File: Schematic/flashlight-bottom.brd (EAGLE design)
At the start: 33.1 x 17.8 mm, 0 parts

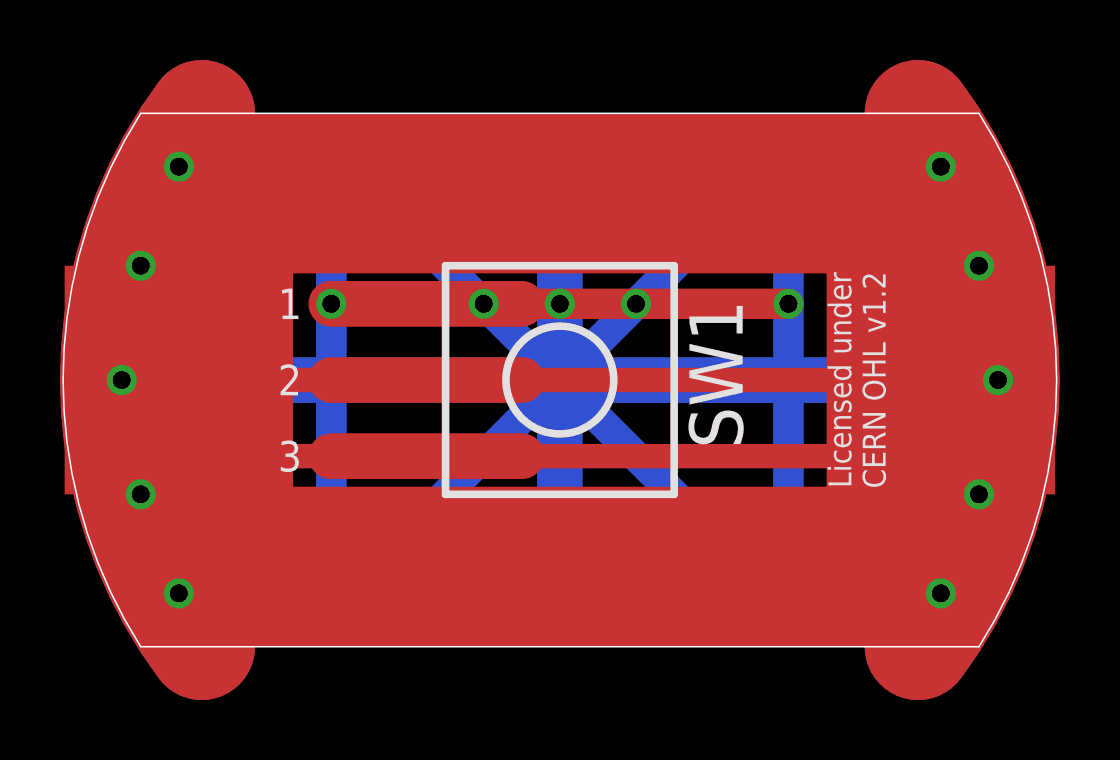
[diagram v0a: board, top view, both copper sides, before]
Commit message: Start revision 3.3 by adding a protection diode.
* Add a protection diode for the current regulator.
* Adjust the footprint of the switch to make it slightly easier
  to position and solder.
* Add text for the Diode to the documentation; however it should
  have updated pictures for the board throughout since this is
  more than a cosmetic change.
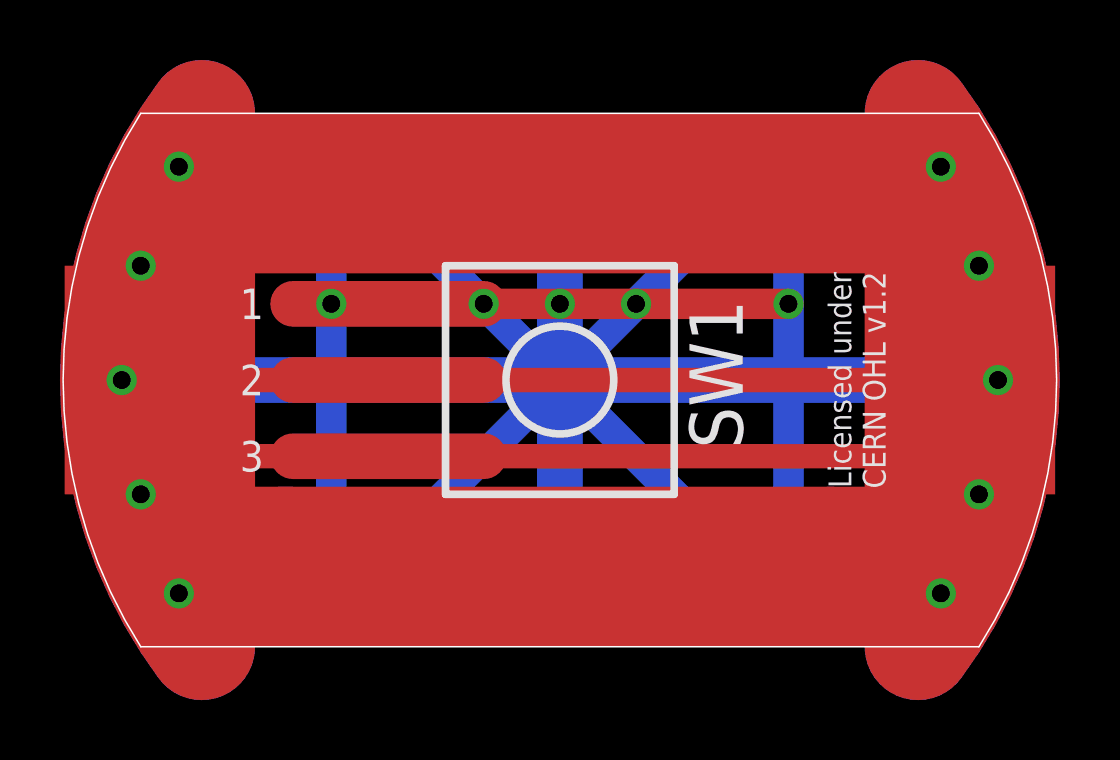
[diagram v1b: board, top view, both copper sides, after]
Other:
- board text added: "Bottom Board Rev. 3.3"
- board text removed: "Bottom Board Rev. 3.2"
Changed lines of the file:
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@@
 <?xml version="1.0" encoding="utf-8"?>
 <!DOCTYPE eagle SYSTEM "eagle.dtd">
-<eagle version="7.2.0">
+<eagle version="7.3.0">
 <drawing>
 <settings>
@@
 Flashlight</text>
 <text x="16.51" y="0.508" size="1.778" layer="29" ratio="15" align="bottom-center">Bottom Board
-Rev. 3.2</text>
+Rev. 3.3</text>
 <wire x1="16.51" y1="8.89" x2="8.89" y2="16.51" width="1.016" layer="30"/>
 <wire x1="16.51" y1="8.89" x2="5.08" y2="8.89" width="1.524" layer="30"/>
@@
 <wire x1="16.51" y1="8.89" x2="16.51" y2="1.905" width="1.524" layer="30"/>
 <circle x="16.51" y="8.89" radius="6.35" width="0.254" layer="22"/>
-<rectangle x1="25.4" y1="5.08" x2="33.02" y2="12.7" layer="1"/>
+<rectangle x1="26.67" y1="5.08" x2="33.02" y2="12.7" layer="1"/>
 <rectangle x1="27.94" y1="5.08" x2="33.02" y2="12.7" layer="29"/>
 <rectangle x1="0" y1="5.08" x2="5.08" y2="12.7" layer="29"/>
-<rectangle x1="0" y1="5.08" x2="7.62" y2="12.7" layer="1"/>
+<rectangle x1="0" y1="5.08" x2="6.35" y2="12.7" layer="1"/>
 <wire x1="2.54" y1="17.78" x2="2.54" y2="0" width="0.0508" layer="20" curve="64.94"/>
 <wire x1="30.48" y1="0" x2="30.48" y2="17.78" width="0.0508" layer="20" curve="64.94"/>
@@
 <wire x1="16.51" y1="8.89" x2="8.89" y2="1.27" width="1.016" layer="30"/>
 <wire x1="16.51" y1="8.89" x2="24.13" y2="1.27" width="1.016" layer="30"/>
-<wire x1="8.89" y1="8.89" x2="15.24" y2="8.89" width="1.524" layer="29"/>
-<wire x1="8.89" y1="11.43" x2="15.24" y2="11.43" width="1.524" layer="29"/>
-<wire x1="8.89" y1="6.35" x2="15.24" y2="6.35" width="1.524" layer="29"/>
+<wire x1="7.62" y1="8.89" x2="13.97" y2="8.89" width="1.524" layer="29"/>
+<wire x1="7.62" y1="11.43" x2="13.97" y2="11.43" width="1.524" layer="29"/>
+<wire x1="7.62" y1="6.35" x2="13.97" y2="6.35" width="1.524" layer="29"/>
 <wire x1="12.7" y1="12.7" x2="20.32" y2="12.7" width="0.254" layer="25"/>
 <wire x1="20.32" y1="12.7" x2="20.32" y2="5.08" width="0.254" layer="25"/>
@@
 <rectangle x1="7.112" y1="1.27" x2="25.908" y2="5.08" layer="1"/>
 <rectangle x1="7.366" y1="12.7" x2="25.654" y2="16.764" layer="1"/>
-<rectangle x1="7.366" y1="12.446" x2="25.4" y2="12.7" layer="1"/>
+<rectangle x1="7.366" y1="12.446" x2="26.67" y2="12.7" layer="1"/>
 <rectangle x1="7.112" y1="5.08" x2="25.654" y2="5.334" layer="1"/>
 <rectangle x1="3.556" y1="0.762" x2="7.62" y2="5.334" layer="1"/>
@@
 <text x="7.62" y="15.748" size="1.016" layer="22" rot="MR270"> 3x C  battery
  This  end (-)</text>
-<text x="7.112" y="10.922" size="1.016" layer="25">1</text>
-<text x="7.112" y="8.382" size="1.016" layer="25">2</text>
-<text x="7.112" y="5.842" size="1.016" layer="25">3</text>
+<text x="5.842" y="10.922" size="1.016" layer="25">1</text>
+<text x="5.842" y="8.382" size="1.016" layer="25">2</text>
+<text x="5.842" y="5.842" size="1.016" layer="25">3</text>
 <wire x1="25.146" y1="14.732" x2="25.146" y2="15.748" width="0.4064" layer="29"/>
 <wire x1="25.146" y1="15.748" x2="24.384" y2="16.51" width="0.4064" layer="29"/>
@@
 </signal>
 <signal name="N$10">
-<wire x1="5.08" y1="8.89" x2="8.89" y2="8.89" width="0.8128" layer="1"/>
-<wire x1="15.24" y1="8.89" x2="27.94" y2="8.89" width="0.8128" layer="1"/>
-<wire x1="8.89" y1="8.89" x2="15.24" y2="8.89" width="1.524" layer="1"/>
-<wire x1="8.89" y1="6.35" x2="15.24" y2="6.35" width="1.524" layer="1"/>
-<wire x1="8.89" y1="11.43" x2="15.24" y2="11.43" width="1.524" layer="1"/>
+<wire x1="5.08" y1="8.89" x2="7.62" y2="8.89" width="0.8128" layer="1"/>
+<wire x1="13.97" y1="8.89" x2="27.94" y2="8.89" width="0.8128" layer="1"/>
+<wire x1="7.62" y1="8.89" x2="13.97" y2="8.89" width="1.524" layer="1"/>
+<wire x1="7.62" y1="6.35" x2="13.97" y2="6.35" width="1.524" layer="1"/>
+<wire x1="7.62" y1="11.43" x2="13.97" y2="11.43" width="1.524" layer="1"/>
 </signal>
 <signal name="N$3">
